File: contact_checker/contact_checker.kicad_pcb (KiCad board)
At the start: 4 copper layers, 160 x 100 mm, 46 parts, among them J1 DB9_Male_Female_Stack_Mountin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, J10 Conn_01x01_Female, J11 Conn_01x01_Female, J12 Conn_01x01_Female, J13 Conn_Triaxial, J14 Conn_Triaxial, J15 Conn_Triaxial, J16 Conn_Triaxial, J17 Conn_01x01_Female, J18 Conn_01x01_Female, J19 Conn_Triaxial, J2 Conn_02x06_Odd_Even, J20 Conn_01x01_Female, J21 Conn_01x01_Female, J22 Conn_01x01_Female, J23 Conn_01x01_Female, J24 Conn_01x01_Female, J25 Conn_Triaxial, J26 RJ45_Shielded, J27 RJ45_Shielded, J28 Conn_01x08, J29 Conn_02x04_Odd_Even, J3 Conn_Coaxial, J30 Conn_01x03, J31 Conn_02x03_Odd_Even, J32 Conn_02x03_Odd_Even, J33 Conn_Coaxial, J34 Conn_Coaxial, J35 Conn_Coaxial, J36 Conn_01x03, J4 Conn_Triaxial, J5 Conn_01x01_Female, J6 Conn_01x01_Female, J7 Conn_Triaxial, J8 Conn_01x01_Female, J9 Conn_01x01_Female, K1 EC2-5NU, K2 EC2-5NU

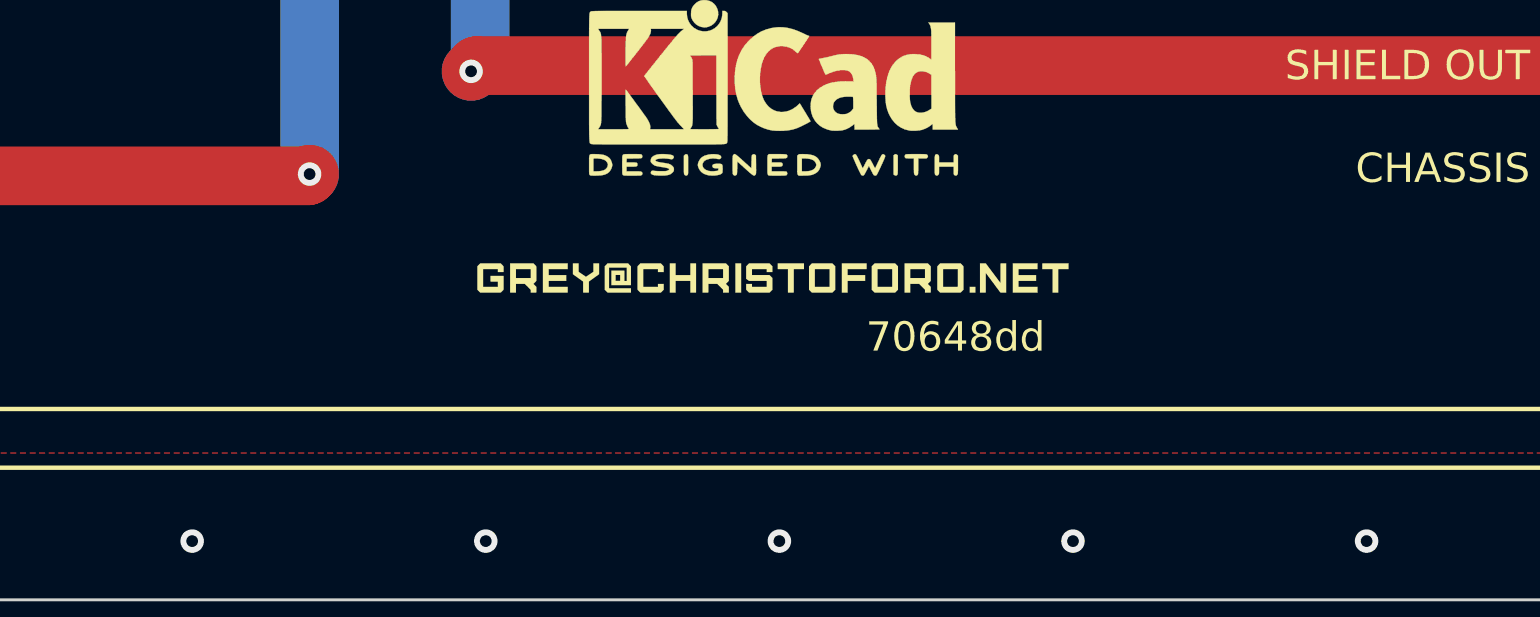
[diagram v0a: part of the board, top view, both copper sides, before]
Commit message: add some missing copper
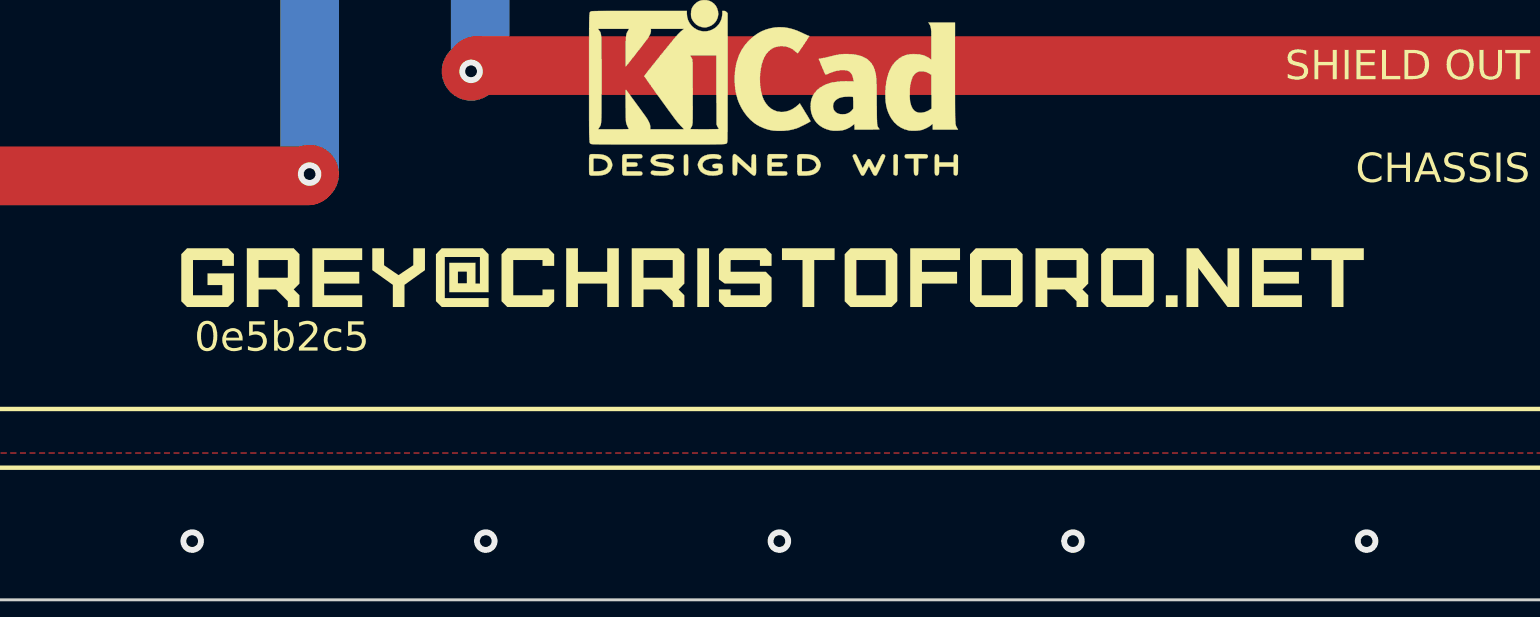
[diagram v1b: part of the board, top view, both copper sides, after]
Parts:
- LOGO1, LOGO2: footprint custom_footprints:logo_small -> custom_footprints:logo
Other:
- board text added: "0e5b2c5"
- board text removed: "70648dd"

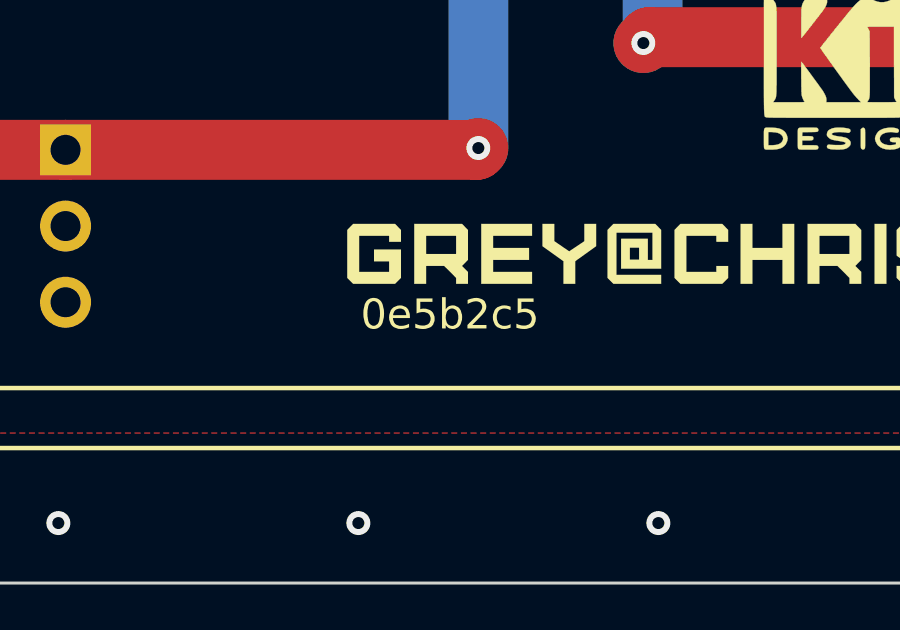
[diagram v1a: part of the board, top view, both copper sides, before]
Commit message: add some missing silkscreen
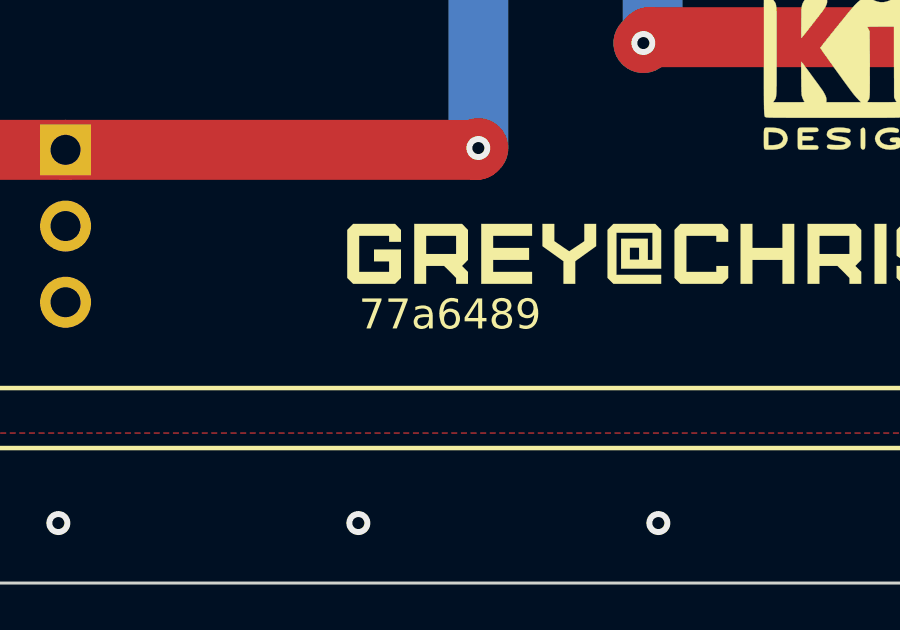
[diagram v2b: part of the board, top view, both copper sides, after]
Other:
- board text added: "77a6489"
- board text removed: "0e5b2c5"
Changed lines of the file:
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@@
     (effects (font (size 1 1) (thickness 0.15)) (justify mirror))
   )
-  (gr_text "0e5b2c5" (at 167.055 138) (layer "B.SilkS")
+  (gr_text "77a6489" (at 167.055 138) (layer "B.SilkS")
     (effects (font (size 1 1) (thickness 0.15)) (justify mirror))
   )
@@
     (effects (font (size 1 1) (thickness 0.15)) (justify left))
   )
-  (gr_text "0e5b2c5" (at 167.055 138.05) (layer "F.SilkS")
+  (gr_text "77a6489" (at 167.055 138.05) (layer "F.SilkS")
     (effects (font (size 1 1) (thickness 0.15)))
   )

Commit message: update silk
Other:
- board text added: "c5b4c2a"
- board text removed: "77a6489"
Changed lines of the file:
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@@
     (effects (font (size 1 1) (thickness 0.15)) (justify mirror))
   )
-  (gr_text "77a6489" (at 167.055 138) (layer "B.SilkS")
+  (gr_text "c5b4c2a" (at 167.055 138) (layer "B.SilkS")
     (effects (font (size 1 1) (thickness 0.15)) (justify mirror))
   )
@@
     (effects (font (size 1 1) (thickness 0.15)) (justify left))
   )
-  (gr_text "77a6489" (at 167.055 138.05) (layer "F.SilkS")
+  (gr_text "c5b4c2a" (at 167.055 138.05) (layer "F.SilkS")
     (effects (font (size 1 1) (thickness 0.15)))
   )

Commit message: contact checker fixups
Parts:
- removed REF** (x2): KiCad-Logo2_5mm_SilkScreen, Symbol:KiCad-Logo2_5mm_SilkScreen
- added R2: 5R, Resistor_SMD:R_2512_6332Metric_Pad1.40x3.35mm_HandSolder, F.Cu at (125.0, 96.7)
- added R3: 5R, Resistor_SMD:R_2512_6332Metric_Pad1.40x3.35mm_HandSolder, F.Cu at (125.0, 104.3)
- added R4: 5R, Resistor_SMD:R_2512_6332Metric_Pad1.40x3.35mm_HandSolder, F.Cu at (125.0, 108.1)
- added R5: 5R, Resistor_SMD:R_2512_6332Metric_Pad1.40x3.35mm_HandSolder, F.Cu at (125.0, 111.9)
- JP3: moved to F.Cu
- LOGO1, LOGO2: footprint custom_footprints:logo -> custom_footprints:site_small
- R1: value 1R -> 5R
- moved J13 25.2 mm to (126.3, 137.3)
- moved JP3 20.8 mm to (124.4, 115.7)
- moved LOGO1 4.28 mm to (187.2, 138.6)
- moved LOGO2 4.28 mm to (187.2, 138.6)
- moved J26 4.04 mm to (206.0, 63.5)
- moved J27 4.04 mm to (72.0, 63.5)
- moved J29 1.20 mm to (205.3, 85.0)
- moved J2 1.08 mm to (73.0, 77.0)
- moved J14 0.31 mm to (123.7, 137.3)
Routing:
- net /IN_LO_FORCE: track 112.7 -> 143.9 mm, vias 6 -> 5
- net Net-(J34-In): track 65.9 -> 84.6 mm
- net /GUARD_SENSE: track 301.2 -> 316.7 mm
- net /GUARD: track 287.0 -> 276.8 mm
- net /IN_LO_SENSE: track 159.6 -> 149.8 mm
- net /OUT_SHIELD: track 210.2 -> 219.0 mm
- net /OUT_LO_FORCE: track 263.7 -> 257.6 mm
- net /OUT_LO_SENSE: track 231.6 -> 236.8 mm
- net /IN_HI_FORCE: track 163.6 -> 168.0 mm
- net /IN_HI_SENSE: track 146.1 -> 150.1 mm
- net /OUT_HI_SENSE: track 255.2 -> 257.8 mm
- net /OUT_HI_FORCE: track 174.9 -> 177.0 mm
- net /IN_SHIELD: track 79.4 -> 81.4 mm
- net +5V: track 154.3 -> 154.8 mm

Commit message: update silk
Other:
- board text added: "93de3f9"
- board text removed: "c5b4c2a"
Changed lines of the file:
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@@
     (effects (font (size 1 1) (thickness 0.15)) (justify mirror))
   )
-  (gr_text "c5b4c2a" (at 201.2 138.6) (layer "B.SilkS")
+  (gr_text "93de3f9" (at 201.2 138.6) (layer "B.SilkS")
     (effects (font (size 1 1) (thickness 0.15)) (justify mirror))
   )
@@
     (effects (font (size 1 1) (thickness 0.15)) (justify left))
   )
-  (gr_text "c5b4c2a" (at 201.2 138.65) (layer "F.SilkS")
+  (gr_text "93de3f9" (at 201.2 138.65) (layer "F.SilkS")
     (effects (font (size 1 1) (thickness 0.15)))
   )

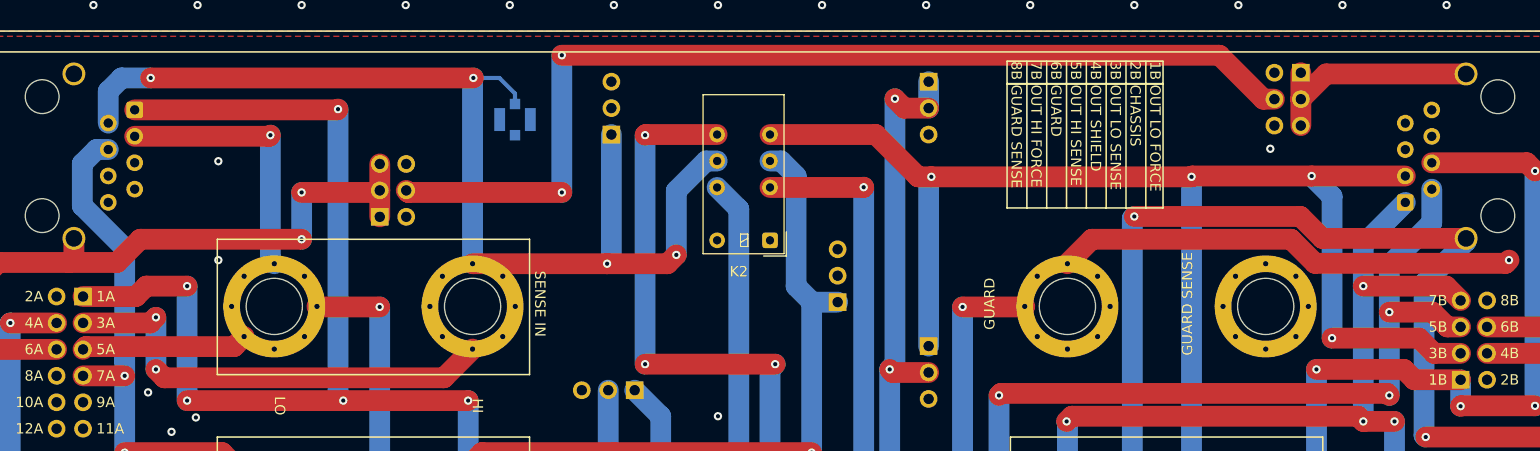
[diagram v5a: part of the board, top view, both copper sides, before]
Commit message: fix up rj45 pad numbering
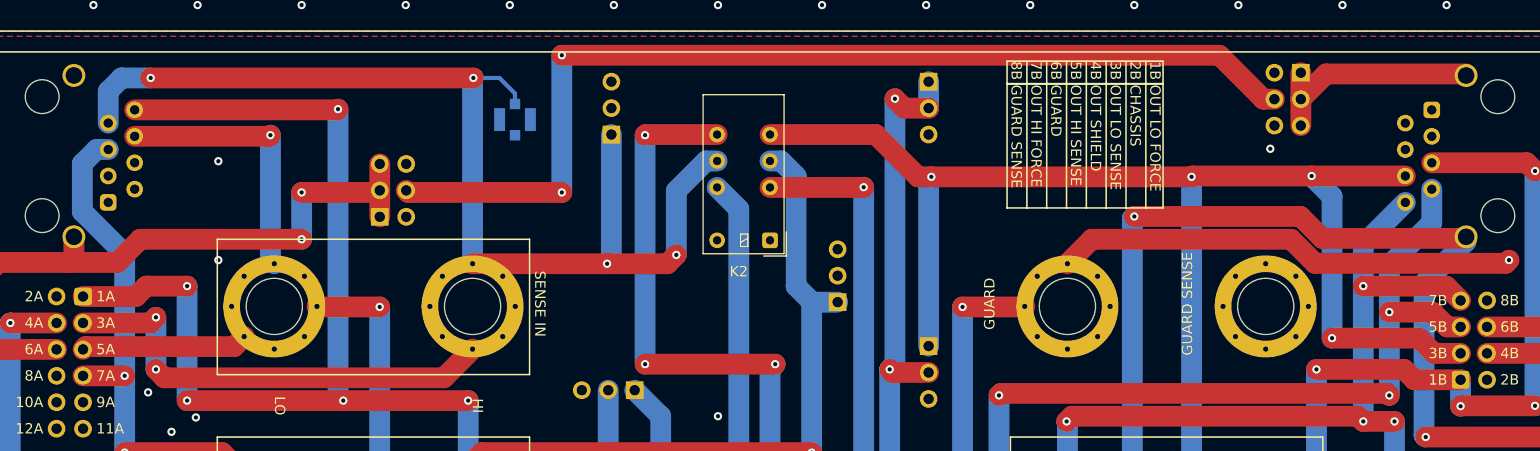
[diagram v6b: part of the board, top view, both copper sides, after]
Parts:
- J2: footprint Connector_PinHeader_2.54mm:PinHeader_2x06_P2.54mm_Horizontal -> Connector_IDC:IDC-Header_2x06_P2.54mm_Horizontal
- J26, J27: footprint custom_footprints:RJ45_WURTH_615008142621_horizontal_shield -> custom_footprints:RJ45_WURTH_615008142621
- J29: footprint Connector_PinHeader_2.54mm:PinHeader_2x04_P2.54mm_Horizontal -> Connector_IDC:IDC-Header_2x04_P2.54mm_Horizontal
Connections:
- J26 pad 1: /OUT_HI_FORCE -> GNDPWR
- J26 pad 2: /OUT_HI_SENSE -> GNDPWR
- J26 pad 3: /OUT_LO_SENSE -> /GUARD
- J26 pad 4: /OUT_LO_FORCE -> /GUARD_SENSE
- J26 pad 5: /GUARD_SENSE -> /OUT_LO_FORCE
- J26 pad 6: /GUARD -> /OUT_LO_SENSE
- J26 pad 7: GNDPWR -> /OUT_HI_SENSE
- J26 pad 8: GNDPWR -> /OUT_HI_FORCE
- J27 pad 1: /IN_HI_FORCE -> GNDPWR
- J27 pad 2: /IN_HI_SENSE -> GNDPWR
- J27 pad 3: /IN_LO_SENSE -> /GUARD
- J27 pad 4: /IN_LO_FORCE -> /GUARD_SENSE
- J27 pad 5: /GUARD_SENSE -> /IN_LO_FORCE
- J27 pad 6: /GUARD -> /IN_LO_SENSE
- J27 pad 7: GNDPWR -> /IN_HI_SENSE
- J27 pad 8: GNDPWR -> /IN_HI_FORCE

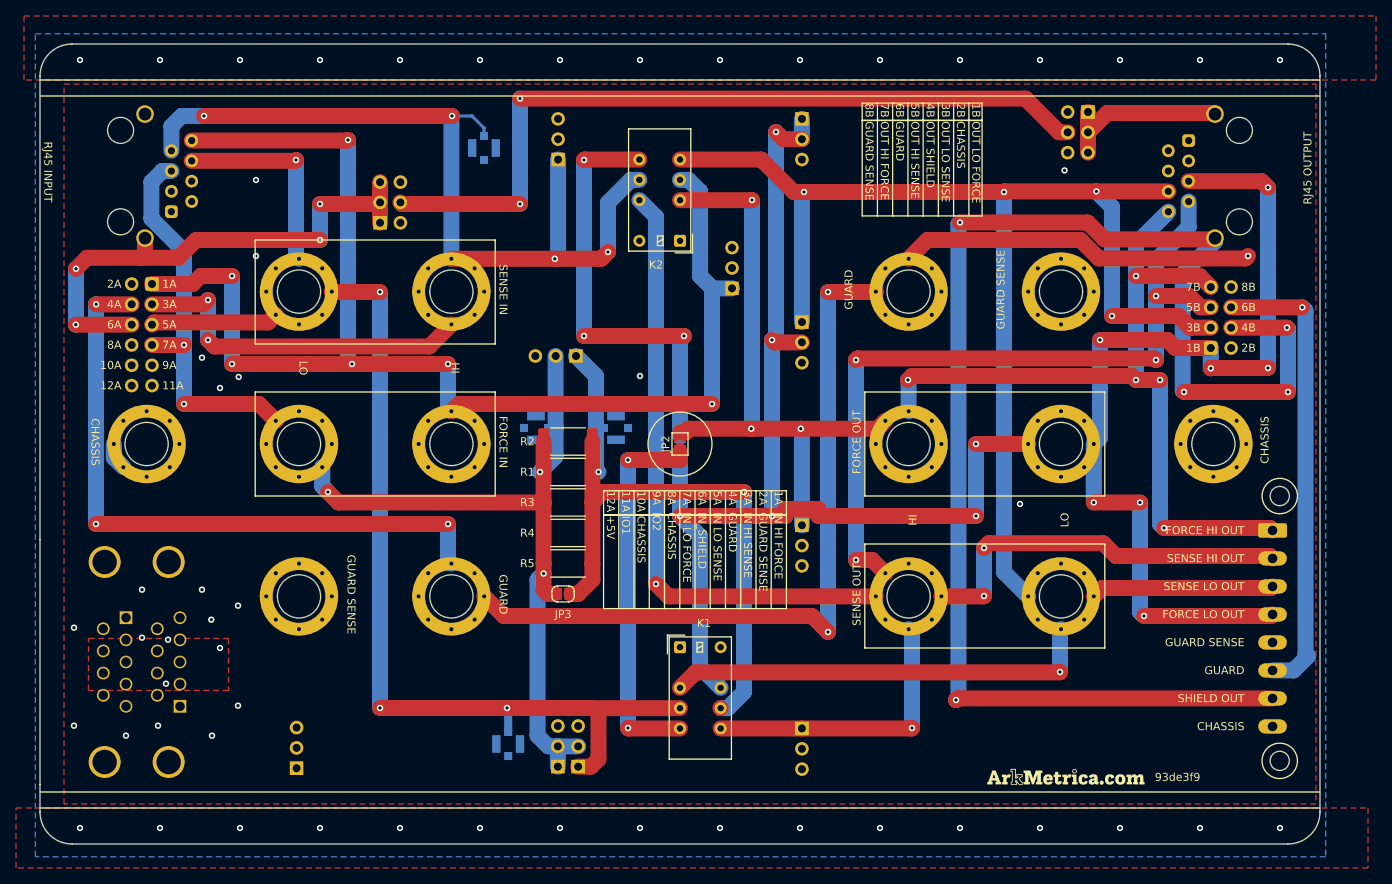
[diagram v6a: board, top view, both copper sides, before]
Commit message: switch contact checker's rj45 part
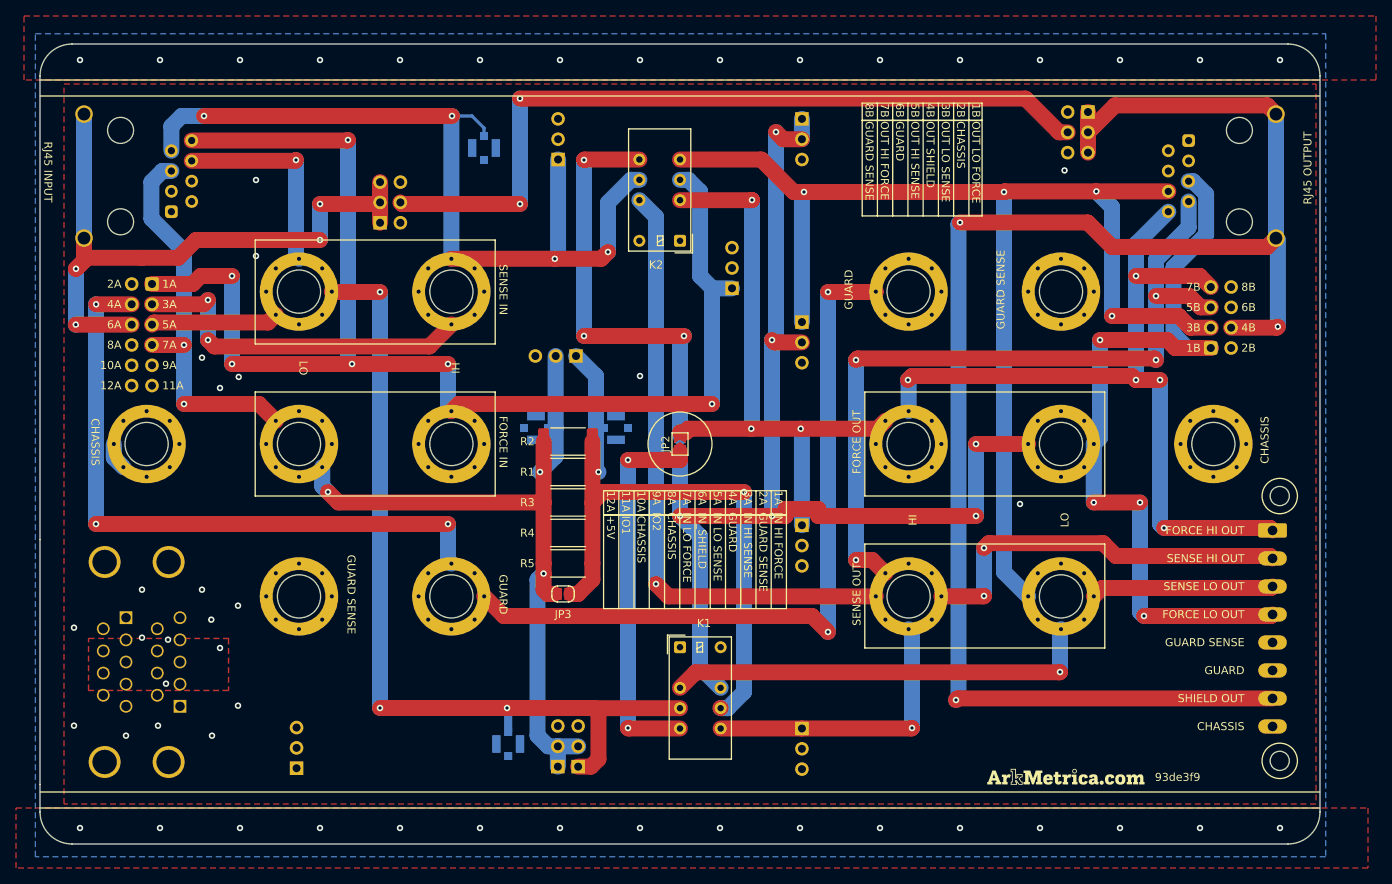
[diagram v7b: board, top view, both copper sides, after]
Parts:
- J26, J27: footprint custom_footprints:RJ45_WURTH_615008142621 -> custom_footprints:RJ45_WURTH_61500814221
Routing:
- net /GUARD: track 276.8 -> 174.4 mm, vias 7 -> 5
- net /OUT_SHIELD: track 219.0 -> 203.7 mm, vias 5 -> 3
- net /OUT_LO_FORCE: track 257.6 -> 242.5 mm, vias 13 -> 10
- net /IN_SHIELD: track 81.4 -> 82.9 mm
